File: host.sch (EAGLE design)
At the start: 127 parts, among them IC1 74LVC1T45GS,132, IC10 74LVC1T45GS,132, IC11 74LVC1T45GS,132, IC12 MMBT3904T, IC2 NCP187AMT120TAG, IC3 LD39200PU33R, IC4 74LVC1T45GS,132, IC5 74LVC1T45GS,132, IC6 74LVC1T45GS,132, IC7 74ALVC164245DGG:11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

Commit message: sync
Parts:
- U$1: USE (none) -> T8Q144I4
- UHDMI: USE (none) -> 10118241-001RLF
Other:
- note added: "+3V3"
- note added: "+5V"
- note added: "0.035mm"
- note added: "0.21mm pre-preg"
- note added: "0.2mm core"
- note added: "Dielectric constant: 4.29 See https://www.pcbway.com/multi-layer-laminated-structure.html"
- note added: "GND"
- note added: "Layer stack-up"
- note added: "Signal"
- moved on the sheet: H1, H2
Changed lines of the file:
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@@
 <setting verticaltext="up"/>
 </settings>
-<grid distance="0.1" unitdist="inch" unit="inch" style="lines" multiple="1" display="yes" altdistance="0.01" altunitdist="inch" altunit="inch"/>
+<grid distance="0.1" unitdist="inch" unit="inch" style="lines" multiple="1" display="no" altdistance="0.01" altunitdist="inch" altunit="inch"/>
 <layers>
 <layer number="1" name="Top" color="4" fill="1" visible="no" active="no"/>
@@
 <part name="FRAME2" library="frames" library_urn="urn:adsk.eagle:library:229" deviceset="A3L-LOC" device=""/>
 <part name="FRAME3" library="frames" library_urn="urn:adsk.eagle:library:229" deviceset="A3L-LOC" device=""/>
-<part name="U$1" library="sjg-efinix" deviceset="T8" device=""/>
+<part name="U$1" library="sjg-efinix" deviceset="T8" device="">
+<attribute name="USE" value="T8Q144I4"/>
+</part>
 <part name="TTAG" library="x-pi" deviceset="TTAG_M" device="_2.00"/>
 <part name="U$2" library="host" deviceset="XE_PBI" device=""/>
@@
 <attribute name="USE" value="CR0201-JW-103GLF"/>
 </part>
-<part name="UHDMI" library="host" deviceset="10118241-001RLF" device=""/>
+<part name="UHDMI" library="host" deviceset="10118241-001RLF" device="">
+<attribute name="USE" value="10118241-001RLF"/>
+</part>
 <part name="DBG_CART" library="pinhead-2" deviceset="PINHD-2X15" device="_2.54"/>
 <part name="DBG_EXT" library="pinhead-2" deviceset="PINHD-2X07" device="_2.54"/>
@@
 [x]        All T8 checklist items
 [x]        Directionality of level xlators</text>
+<wire x1="316.865" y1="52.705" x2="347.345" y2="52.705" width="1.27" layer="94"/>
+<text x="349.885" y="59.817" size="1.778" layer="94">0.035mm</text>
+<text x="349.885" y="52.197" size="1.778" layer="94">0.035mm</text>
+<text x="295.91" y="99.06" size="1.778" layer="94">Layer stack-up</text>
+<wire x1="290.83" y1="104.14" x2="382.27" y2="104.14" width="0.2032" layer="94"/>
+<wire x1="382.27" y1="104.14" x2="382.27" y2="30.48" width="0.2032" layer="94"/>
+<wire x1="382.27" y1="30.48" x2="290.83" y2="30.48" width="0.2032" layer="94"/>
+<wire x1="290.83" y1="30.48" x2="290.83" y2="104.14" width="0.2032" layer="94"/>
+<text x="314.96" y="68.58" size="1.778" layer="94" rot="R180">+3V3</text>
+<text x="294.005" y="32.385" size="1.778" layer="94">Dielectric constant: 4.29
+See https://www.pcbway.com/multi-layer-laminated-structure.html</text>
+<text x="314.96" y="76.2" size="1.778" layer="94" rot="R180">Signal</text>
+<wire x1="316.865" y1="60.325" x2="347.345" y2="60.325" width="1.27" layer="94"/>
+<wire x1="316.865" y1="67.945" x2="347.345" y2="67.945" width="1.27" layer="94"/>
+<wire x1="316.865" y1="75.565" x2="347.345" y2="75.565" width="1.27" layer="94"/>
+<text x="349.885" y="67.437" size="1.778" layer="94">0.035mm</text>
+<text x="349.885" y="75.057" size="1.778" layer="94">0.035mm</text>
+<text x="314.96" y="60.96" size="1.778" layer="94" rot="R180">GND</text>
+<text x="314.96" y="53.34" size="1.778" layer="94" rot="R180">Signal </text>
+<text x="314.96" y="83.82" size="1.778" layer="94" rot="R180">+5V</text>
+<text x="314.96" y="91.44" size="1.778" layer="94" rot="R180">Signal</text>
+<wire x1="316.865" y1="83.185" x2="347.345" y2="83.185" width="1.27" layer="94"/>
+<wire x1="316.865" y1="90.805" x2="347.345" y2="90.805" width="1.27" layer="94"/>
+<text x="349.885" y="82.677" size="1.778" layer="94">0.035mm</text>
+<text x="349.885" y="90.297" size="1.778" layer="94">0.035mm</text>
+<text x="324.485" y="85.725" size="1.778" layer="94">0.21mm pre-preg</text>
+<text x="324.485" y="78.105" size="1.778" layer="94">0.2mm core</text>
+<text x="324.485" y="70.485" size="1.778" layer="94">0.21mm pre-preg</text>
+<text x="324.485" y="55.245" size="1.778" layer="94">0.21mm pre-preg</text>
+<text x="324.485" y="62.865" size="1.778" layer="94">0.2mm core</text>
 </plain>
 <instances>
@@
 <attribute name="NAME" x="134.62" y="175.768" size="1.778" layer="95" rot="MR0"/>
 <attribute name="VALUE" x="134.62" y="109.22" size="1.778" layer="96" rot="MR0"/>
+<attribute name="USE" x="116.84" y="144.78" size="1.778" layer="96" rot="MR0" display="off"/>
 </instance>
-<instance part="H1" gate="G$1" x="294.64" y="33.02" smashed="yes">
-<attribute name="NAME" x="297.434" y="33.6042" size="1.778" layer="95"/>
-<attribute name="VALUE" x="297.434" y="30.5562" size="1.778" layer="96"/>
-</instance>
-<instance part="H2" gate="G$1" x="294.64" y="40.64" smashed="yes">
-<attribute name="NAME" x="297.434" y="41.2242" size="1.778" layer="95"/>
-<attribute name="VALUE" x="297.434" y="38.1762" size="1.778" layer="96"/>
+<instance part="H1" gate="G$1" x="116.84" y="86.36" smashed="yes">
+<attribute name="NAME" x="119.634" y="86.9442" size="1.778" layer="95"/>
+<attribute name="VALUE" x="119.634" y="83.8962" size="1.778" layer="96"/>
+</instance>
+<instance part="H2" gate="G$1" x="116.84" y="93.98" smashed="yes">
+<attribute name="NAME" x="119.634" y="94.5642" size="1.778" layer="95"/>
+<attribute name="VALUE" x="119.634" y="91.5162" size="1.778" layer="96"/>
 </instance>
 <instance part="R32" gate="G$1" x="233.68" y="104.14" smashed="yes" rot="R90">
@@
 <attribute name="USE" x="269.24" y="55.88" size="1.778" layer="96" rot="R180" display="off"/>
 </instance>
-<instance part="SUPPLY33" gate="GND" x="281.94" y="20.32" smashed="yes">
-<attribute name="VALUE" x="280.035" y="17.145" size="1.778" layer="96"/>
+<instance part="SUPPLY33" gate="GND" x="104.14" y="73.66" smashed="yes">
+<attribute name="VALUE" x="102.235" y="70.485" size="1.778" layer="96"/>
 </instance>
 </instances>
@@
 <segment>
 <pinref part="SUPPLY33" gate="GND" pin="GND"/>
-<wire x1="281.94" y1="22.86" x2="281.94" y2="33.02" width="0.1524" layer="91"/>
+<wire x1="104.14" y1="76.2" x2="104.14" y2="86.36" width="0.1524" layer="91"/>
 <pinref part="H2" gate="G$1" pin="MOUNT"/>
-<wire x1="281.94" y1="33.02" x2="281.94" y2="40.64" width="0.1524" layer="91"/>
-<wire x1="281.94" y1="40.64" x2="292.1" y2="40.64" width="0.1524" layer="91"/>
+<wire x1="104.14" y1="86.36" x2="104.14" y2="93.98" width="0.1524" layer="91"/>
+<wire x1="104.14" y1="93.98" x2="114.3" y2="93.98" width="0.1524" layer="91"/>
 <pinref part="H1" gate="G$1" pin="MOUNT"/>
-<wire x1="292.1" y1="33.02" x2="281.94" y2="33.02" width="0.1524" layer="91"/>
-<junction x="281.94" y="33.02"/>
+<wire x1="114.3" y1="86.36" x2="104.14" y2="86.36" width="0.1524" layer="91"/>
+<junction x="104.14" y="86.36"/>
 </segment>
 </net>
@@
 <attribute name="NAME" x="276.86" y="79.502" size="1.27" layer="94"/>
 <attribute name="VALUE" x="276.86" y="-12.7" size="1.27" layer="94"/>
+<attribute name="USE" x="294.64" y="35.56" size="1.778" layer="96" display="off"/>
 </instance>
 <instance part="U$5" gate="G$1" x="264.16" y="81.28" smashed="yes">
@@
 </sheet>
 </sheets>
+<errors>
+</errors>
 </schematic>
 </drawing>

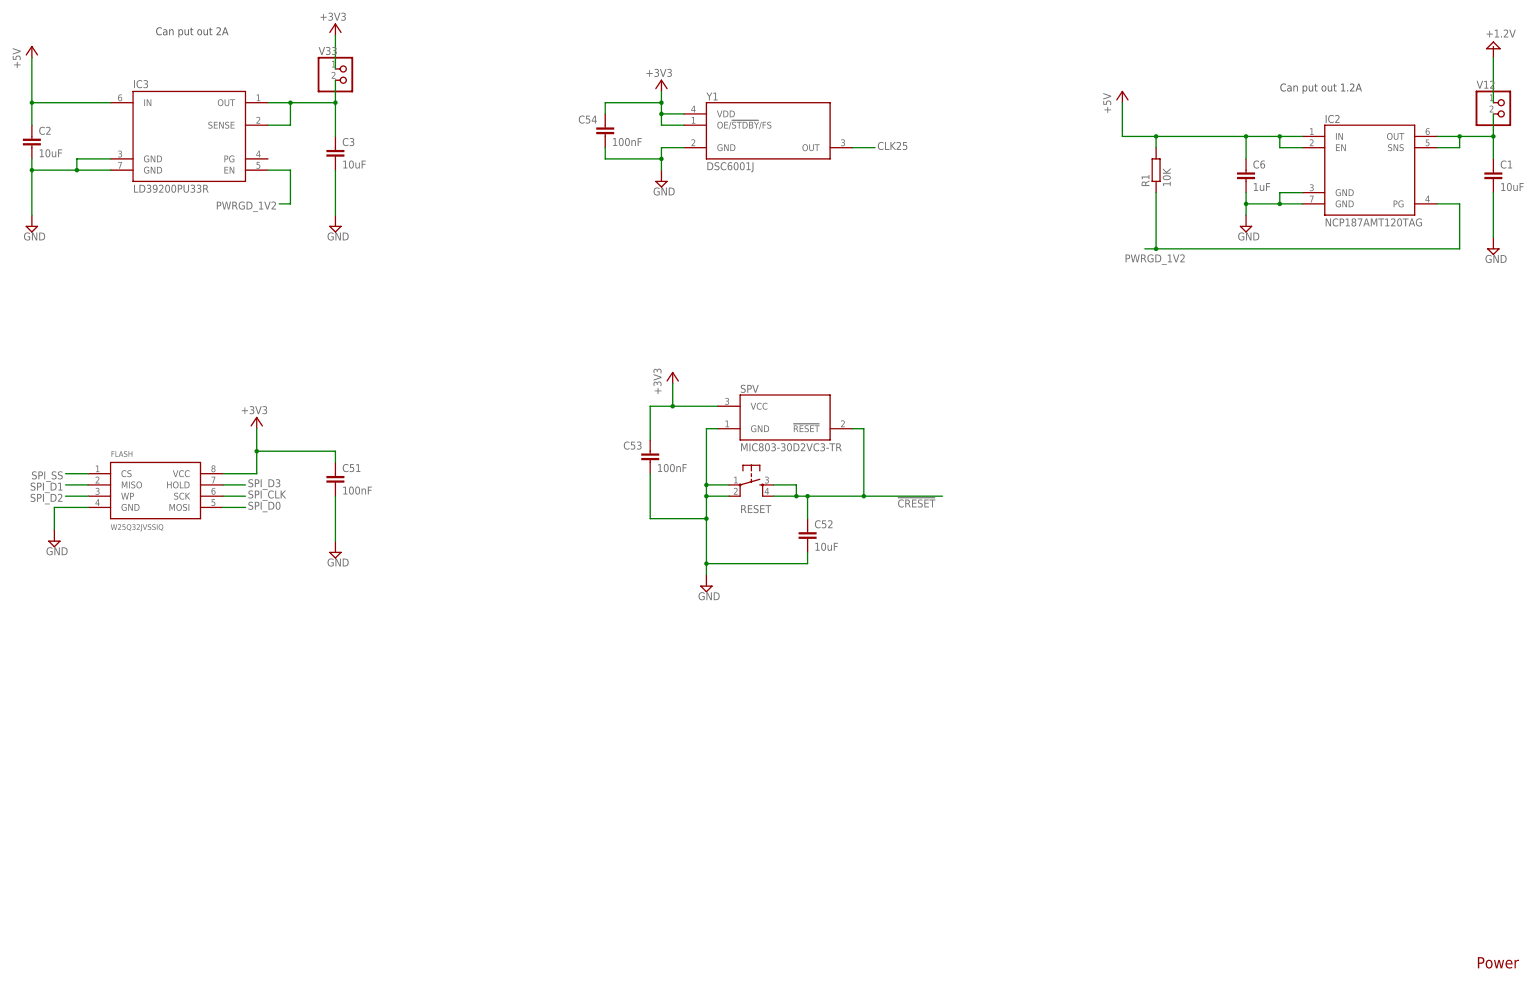
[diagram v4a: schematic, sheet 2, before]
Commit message: Change to available parts
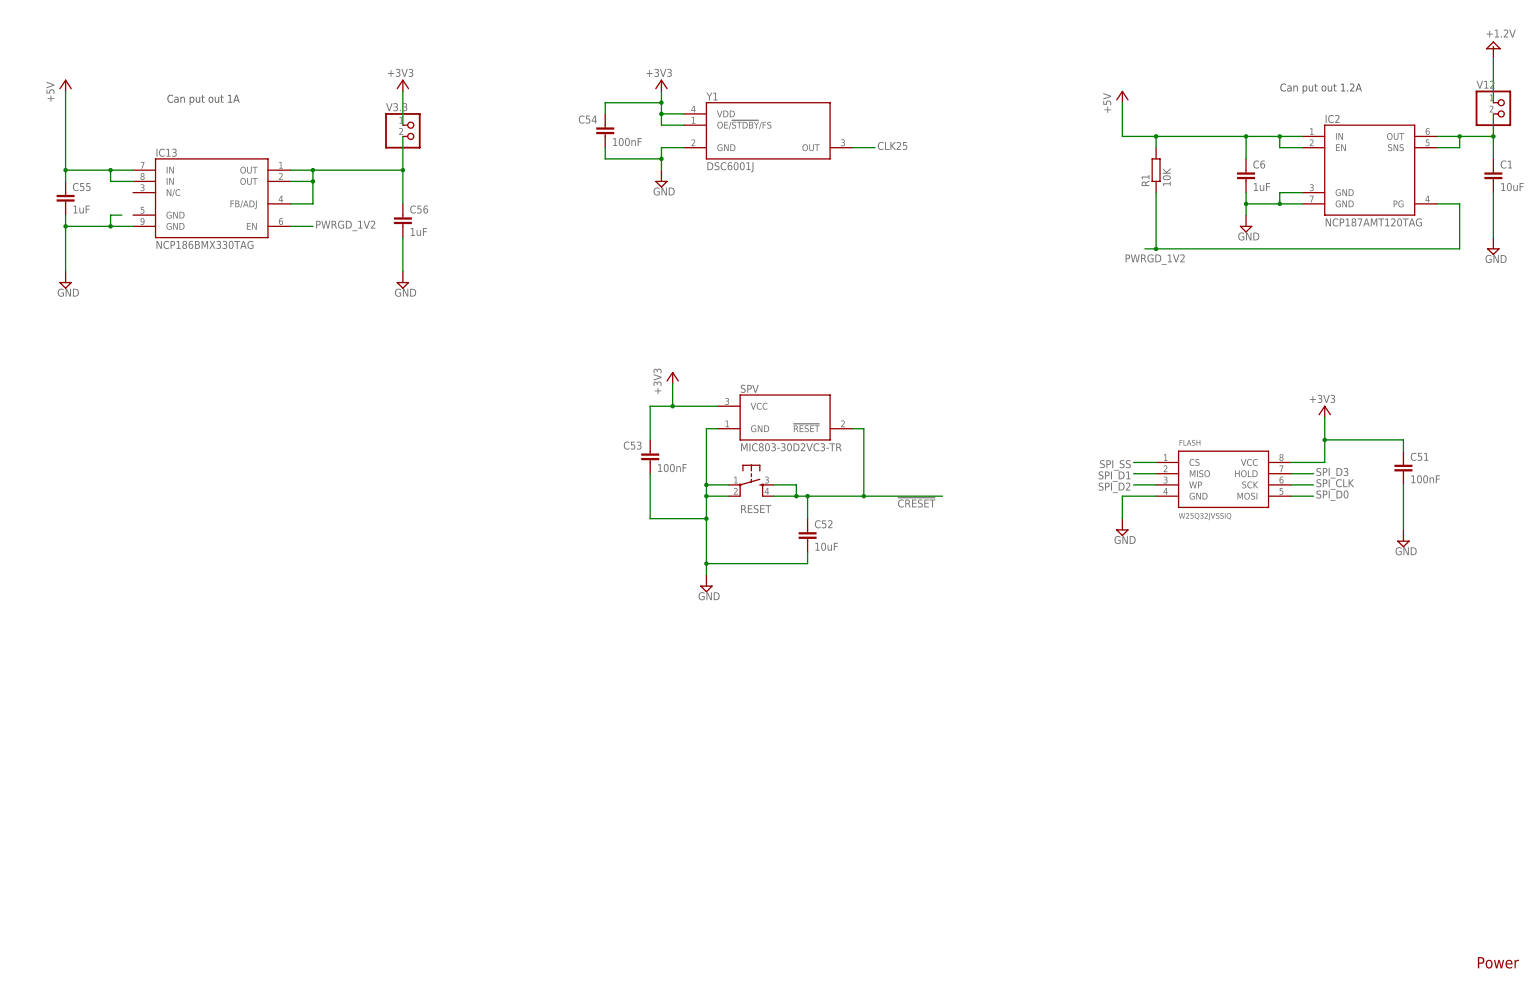
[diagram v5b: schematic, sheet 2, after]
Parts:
- removed C2, C3: 10uF, rcl:C-EUC0402K
- removed IC3: LD39200PU33R, x-pi:LD39200PU33R
- removed V33: (no value), pinhead:PINHD-1X2
- added C55, C56: 1uF, rcl:C-EUC0201
- added IC13: NCP186BMX330TAG, host:NCP186BMX330TAG
- added V3.3: (no value), pinhead:PINHD-1X2
- IC12: value MMBT3904T -> MUN2211T3G
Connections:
- removed net N$4: C3.1, IC3.OUT@1, IC3.SENSE@2, V33.2
- new net N$18: C56.1, IC13.FB/ADJ@4, IC13.OUT@1, IC13.OUT@2, V3.3.2
- net +3V3: now also V3.3.1; no longer V33.1
- net +5V: now also C55.1, IC13.IN@7, IC13.IN@8; no longer C2.1, IC3.IN@6
- net GND: now also C55.2, C56.2, IC13.GND@EPAD; no longer C2.2, C3.2, IC3.GND@3, IC3.GND@PAD
- net PWRGD_1V2: now also IC13.EN@6; no longer IC3.EN@5
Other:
- note added: "Can put out 1A"
- note added: "Checklist: [x] All T8 checklist items [x] Directionality of level xlators To Do: - Swap out the BJT NPN on CDONE with the design from x-pi - Find a replacement 3.3v regulator"
- note removed: "Can put out 2A"
- note removed: "Checklist: [x] All T8 checklist items [x] Directionality of level xlators"
- moved on the sheet: C51, FLASH
